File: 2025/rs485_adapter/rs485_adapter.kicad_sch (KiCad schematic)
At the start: 15 parts, among them J1 USB_C_Receptacle_USB2.0_16P, J2 Screw_Terminal_01x03, U1 CH340E, U2 MAX485E

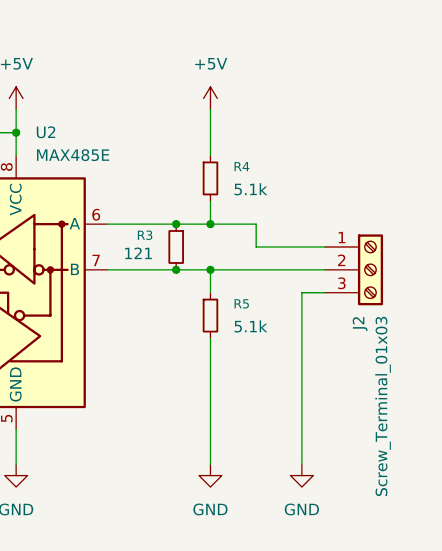
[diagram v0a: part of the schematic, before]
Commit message: Added RS485 naming to schematic
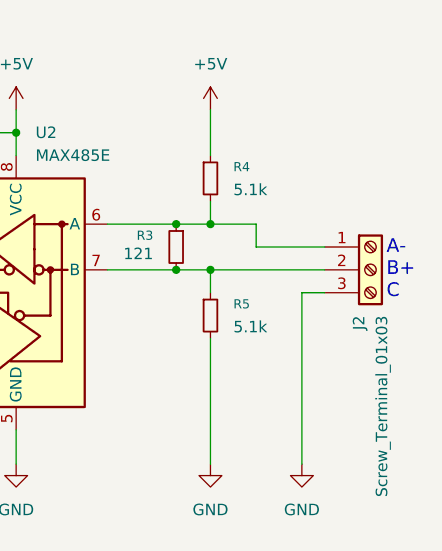
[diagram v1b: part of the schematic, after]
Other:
- note added: "A- B+ C"
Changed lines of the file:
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@@
 	(title_block
 		(title "USB-C to RS485 Converter")
-		(date "2025-11-24")
-		(rev "A")
+		(date "2025-12-10")
+		(rev "A1")
 		(company "Brandon Kirisaki")
 	)
+	(text "A-\nB+\nC"
+		(exclude_from_sim no)
+		(at 260.858 101.6 0)
+		(effects
+			(font
+				(size 1.524 1.524)
+			)
+			(justify left)
+		)
+	)
 	(junction
